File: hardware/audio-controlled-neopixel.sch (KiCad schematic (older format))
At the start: 63 parts, among them J1 AudioJack4, J2 AudioJack4, J3 KF2EDGK, J4 KF2EDGK, J5 KF2EDGK, J6 Conn_01x01_Female, J7 Conn_01x01_Female, J8 Conn_01x01_Female, J9 Conn_01x01_Female, SW1 SW_SPST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

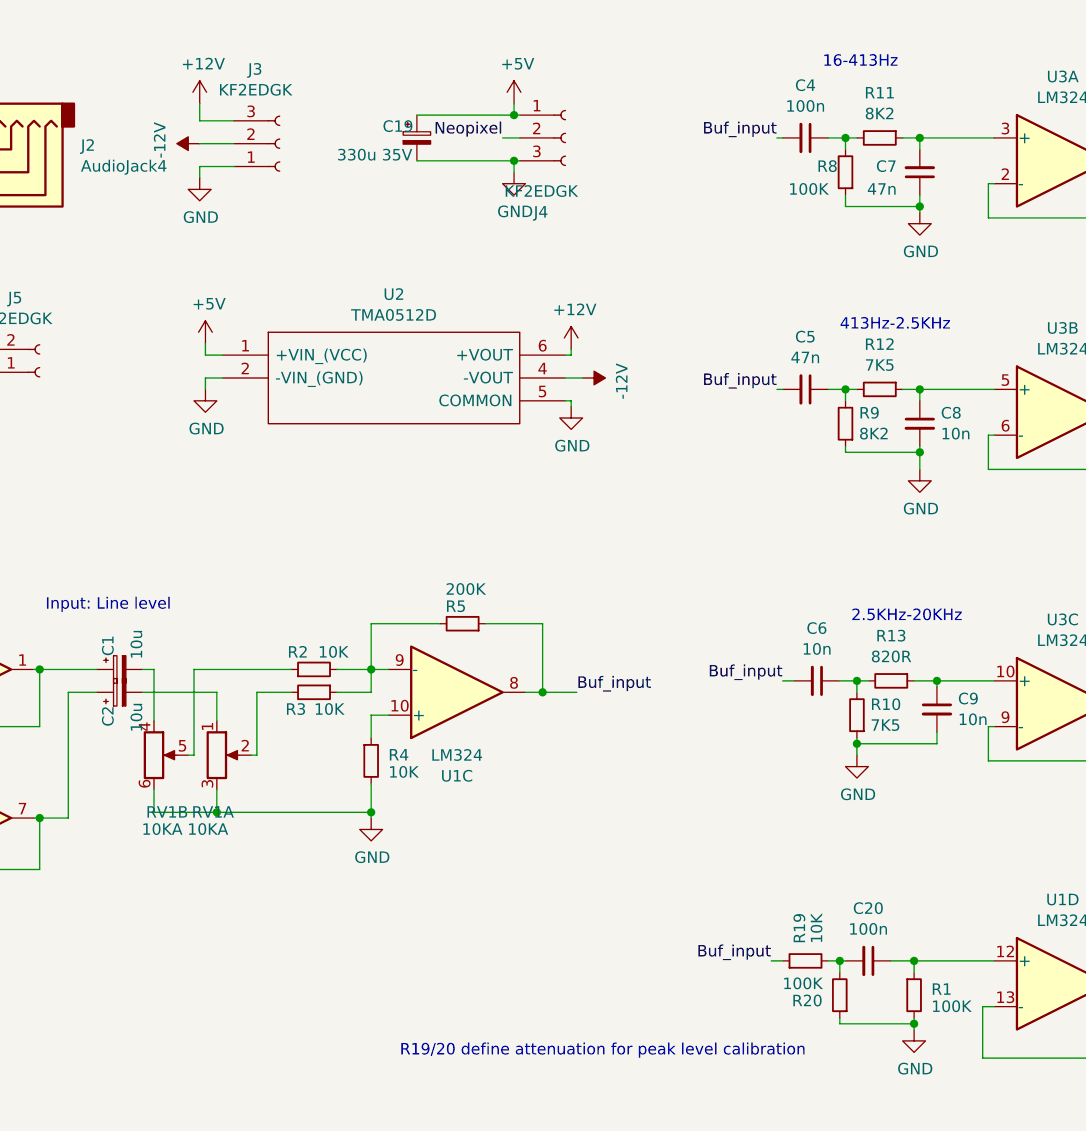
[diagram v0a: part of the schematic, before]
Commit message: added attenuators to keep frequency response flat
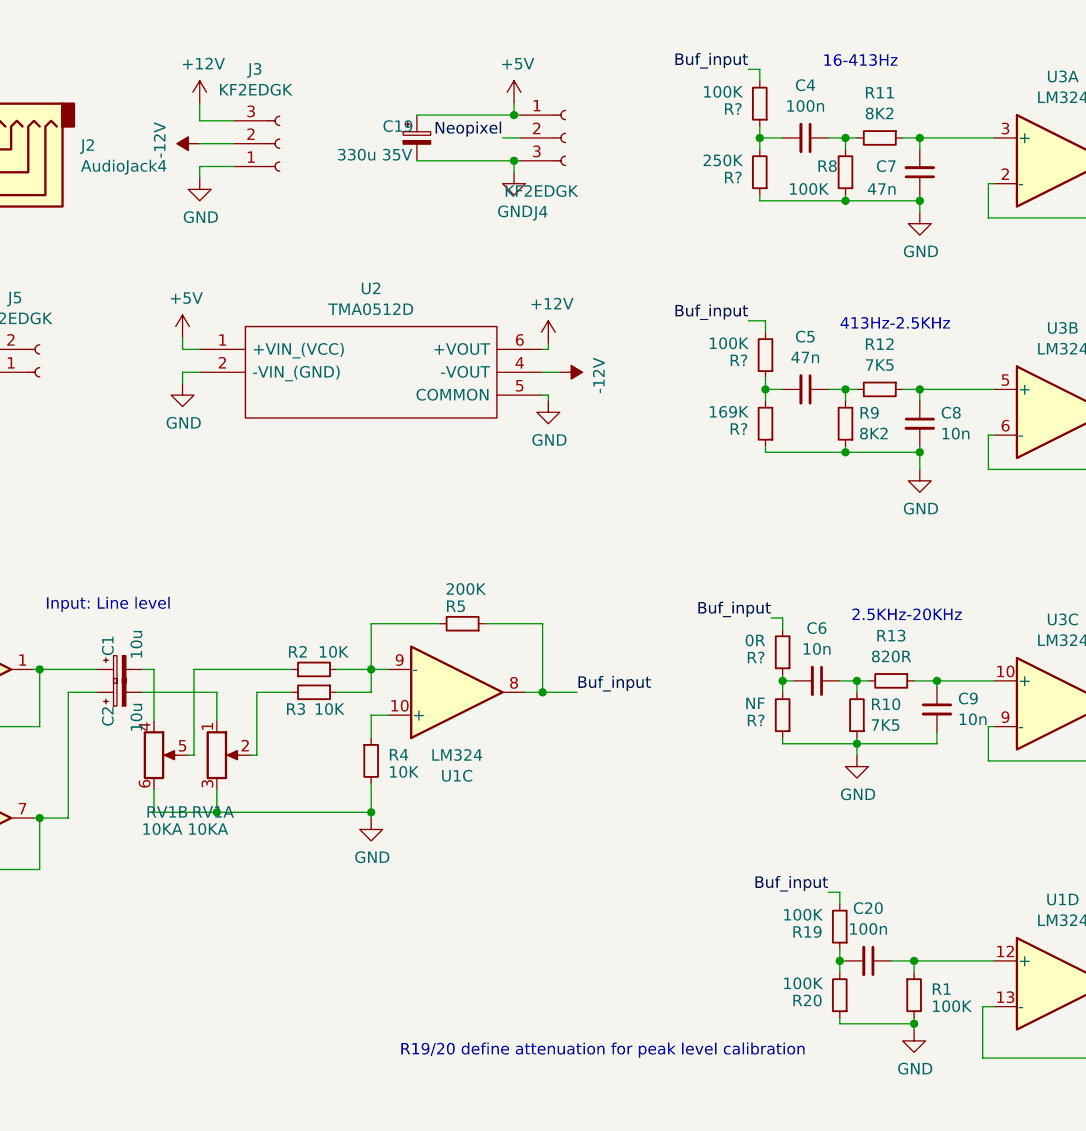
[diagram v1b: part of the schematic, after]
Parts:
- added R?: 0R, Resistor_SMD:R_0805_2012Metric, symbol Device:R_Small
- added R?: NF, Resistor_SMD:R_0805_2012Metric, symbol Device:R_Small
- added R? (x2): 100K, Resistor_SMD:R_0805_2012Metric, symbol Device:R_Small
- added R?: 169K, Resistor_SMD:R_0805_2012Metric, symbol Device:R_Small
- added R?: 250K, Resistor_SMD:R_0805_2012Metric, symbol Device:R_Small
- R19: value 10K -> 100K
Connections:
- net Buf_input: now also R19.2, R?.2, R?.2, R?.2; no longer C4.2, C5.2, C6.2, R19.1
- net GND: now also R?.1, R?.1, R?.1
- net at C20.2, R20.2: now also R19.1; no longer R19.2
- new net: C6.2, R?.1, R?.2
- new net: C5.2, R?.1, R?.2
- new net: C4.2, R?.1, R?.2
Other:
- moved on the sheet: R19, U2

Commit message: fixed library issue with schematic
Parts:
- U2: symbol TMA_2412D:TMA_2412D -> audio-controlled-neopixel-cache:TMA_2412D_TMA_2412D
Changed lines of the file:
@@
 EESchema Schematic File Version 4
+LIBS:audio-controlled-neopixel-cache
 EELAYER 26 0
 EELAYER END
@@
 Connection ~ 1200 1200
 $Comp
-L TMA_2412D:TMA_2412D U2
+L audio-controlled-neopixel-cache:TMA_2412D_TMA_2412D U2
 U 1 1 5C4B4FE3
 P 2450 1875

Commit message: added attenuators to balance frequency response
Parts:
- U2: footprint custom:TMA-0512D -> Footprints:TMAxxxxD; symbol audio-controlled-neopixel-cache:TMA_2412D_TMA_2412D -> audio-controlled-neopixel:custom_TMAxxxxD
- gave numbers to parts that had none: 6
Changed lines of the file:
@@
 L power:+12V #PWR0106
 U 1 1 5BF24254
-P 3975 1850
-F 0 "#PWR0106" H 3975 1700 50  0001 C CNN
-F 1 "+12V" H 3990 2023 50  0000 C CNN
-F 2 "" H 3975 1850 50  0001 C CNN
-F 3 "" H 3975 1850 50  0001 C CNN
-	1    3975 1850
+P 3475 1800
+F 0 "#PWR0106" H 3475 1650 50  0001 C CNN
+F 1 "+12V" H 3490 1973 50  0000 C CNN
+F 2 "" H 3475 1800 50  0001 C CNN
+F 3 "" H 3475 1800 50  0001 C CNN
+	1    3475 1800
 	1    0    0    -1
 $EndComp
@@
 L power:-12V #PWR0107
 U 1 1 5BF242D9
-P 4025 1975
-F 0 "#PWR0107" H 4025 2075 50  0001 C CNN
-F 1 "-12V" H 4040 2148 50  0000 C CNN
-F 2 "" H 4025 1975 50  0001 C CNN
-F 3 "" H 4025 1975 50  0001 C CNN
-	1    4025 1975
+P 3525 1925
+F 0 "#PWR0107" H 3525 2025 50  0001 C CNN
+F 1 "-12V" H 3540 2098 50  0000 C CNN
+F 2 "" H 3525 1925 50  0001 C CNN
+F 3 "" H 3525 1925 50  0001 C CNN
+	1    3525 1925
 	0    1    1    0
 $EndComp
 Wire Wire Line
-	3975 2100 3975 2075
-Wire Wire Line
-	3975 2075 3950 2075
-Wire Wire Line
-	3975 1850 3975 1875
-Wire Wire Line
-	3975 1875 3950 1875
-Wire Wire Line
-	3950 1975 4025 1975
+	3475 2050 3475 2025
+Wire Wire Line
+	3475 2025 3450 2025
+Wire Wire Line
+	3475 1800 3475 1825
+Wire Wire Line
+	3475 1825 3450 1825
+Wire Wire Line
+	3450 1925 3525 1925
 $Comp
 L Diode:BAT85 D3
@@
 L power:GND #PWR0111
 U 1 1 5C0E2BC2
-P 3975 2100
-F 0 "#PWR0111" H 3975 1850 50  0001 C CNN
-F 1 "GND" H 3980 1927 50  0000 C CNN
-F 2 "" H 3975 2100 50  0001 C CNN
-F 3 "" H 3975 2100 50  0001 C CNN
-	1    3975 2100
+P 3475 2050
+F 0 "#PWR0111" H 3475 1800 50  0001 C CNN
+F 1 "GND" H 3480 1877 50  0000 C CNN
+F 2 "" H 3475 2050 50  0001 C CNN
+F 3 "" H 3475 2050 50  0001 C CNN
+	1    3475 2050
 	1    0    0    -1
 $EndComp
@@
 	1400 1200 1200 1200
 Connection ~ 1200 1200
-$Comp
-L audio-controlled-neopixel-cache:TMA_2412D_TMA_2412D U2
-U 1 1 5C4B4FE3
-P 2450 1875
-F 0 "U2" H 3200 2140 50  0000 C CNN
-F 1 "TMA0512D" H 3200 2049 50  0000 C CNN
-F 2 "custom:TMA-0512D" H 3800 1975 50  0001 L CNN
-F 3 "http://docs-emea.rs-online.com/webdocs/0e18/0900766b80e182f0.pdf" H 3800 1875 50  0001 L CNN
-F 4 "TMA2412D unregulated DC-DC,+/-12V 1W 1W Isolated DC-DC Converter, Vin 21.6" H 3800 1775 50  0001 L CNN "Description"
-F 5 "Traco Power" H 3800 1575 50  0001 L CNN "Manufacturer_Name"
-F 6 "TMA 2412D" H 3800 1475 50  0001 L CNN "Manufacturer_Part_Number"
-F 7 "1247598" H 3800 1375 50  0001 L CNN "RS Part Number"
-F 8 "http://uk.rs-online.com/web/p/products/1247598" H 3800 1275 50  0001 L CNN "RS Price/Stock"
-F 9 "495-TMA-2412D" H 3800 1175 50  0001 L CNN "Mouser Part Number"
-F 10 "https://www.mouser.com/Search/Refine.aspx?Keyword=495-TMA-2412D" H 3800 1075 50  0001 L CNN "Mouser Price/Stock"
-	1    2450 1875
-	1    0    0    -1
-$EndComp
 Text Label 4950 3050 2    50   ~ 0
 Buf_input
 $Comp
-L Device:R_Small R?
+L Device:R_Small R25
 U 1 1 5C4F25BC
 P 5000 3200
-F 0 "R?" H 5075 3225 50  0000 L CNN
+F 0 "R25" H 5075 3225 50  0000 L CNN
 F 1 "0R" H 5075 3150 50  0000 L CNN
 F 2 "Resistor_SMD:R_0805_2012Metric" H 5000 3200 50  0001 C CNN
@@
 $EndComp
 $Comp
-L Device:R_Small R?
+L Device:R_Small R26
 U 1 1 5C4F25C3
 P 5000 3475
-F 0 "R?" H 5075 3500 50  0000 L CNN
+F 0 "R26" H 5075 3500 50  0000 L CNN
 F 1 "NF" H 5075 3425 50  0000 L CNN
 F 2 "Resistor_SMD:R_0805_2012Metric" H 5000 3475 50  0001 C CNN
@@
 Buf_input
 $Comp
-L Device:R_Small R?
+L Device:R_Small R23
 U 1 1 5C53A2E4
 P 4925 1900
-F 0 "R?" H 5000 1925 50  0000 L CNN
+F 0 "R23" H 5000 1925 50  0000 L CNN
 F 1 "100K" H 5000 1850 50  0000 L CNN
 F 2 "Resistor_SMD:R_0805_2012Metric" H 4925 1900 50  0001 C CNN
@@
 $EndComp
 $Comp
-L Device:R_Small R?
+L Device:R_Small R24
 U 1 1 5C53A2EA
 P 4925 2200
-F 0 "R?" H 5000 2225 50  0000 L CNN
+F 0 "R24" H 5000 2225 50  0000 L CNN
 F 1 "169K" H 5000 2150 50  0000 L CNN
 F 2 "Resistor_SMD:R_0805_2012Metric" H 4925 2200 50  0001 C CNN
@@
 Buf_input
 $Comp
-L Device:R_Small R?
+L Device:R_Small R21
 U 1 1 5C5862DE
 P 4900 800
-F 0 "R?" H 4975 825 50  0000 L CNN
+F 0 "R21" H 4975 825 50  0000 L CNN
 F 1 "100K" H 4975 750 50  0000 L CNN
 F 2 "Resistor_SMD:R_0805_2012Metric" H 4900 800 50  0001 C CNN
@@
 $EndComp
 $Comp
-L Device:R_Small R?
+L Device:R_Small R22
 U 1 1 5C5862E4
 P 4900 1100
-F 0 "R?" H 4975 1125 50  0000 L CNN
+F 0 "R22" H 4975 1125 50  0000 L CNN
 F 1 "250K" H 4975 1050 50  0000 L CNN
 F 2 "Resistor_SMD:R_0805_2012Metric" H 4900 1100 50  0001 C CNN
@@
 Wire Wire Line
 	5250 4250 5250 4300
+$Comp
+L audio-controlled-neopixel:custom_TMAxxxxD U2
+U 1 1 5C4B4FE3
+P 2950 2075
+F 0 "U2" H 2775 1725 50  0000 C CNN
+F 1 "TMA0512D" H 3025 1950 50  0000 C CNN
+F 2 "Footprints:TMAxxxxD" H 4300 2175 50  0001 L CNN
+F 3 "http://docs-emea.rs-online.com/webdocs/0e18/0900766b80e182f0.pdf" H 4300 2075 50  0001 L CNN
+F 4 "TMA2412D unregulated DC-DC,+/-12V 1W 1W Isolated DC-DC Converter, Vin 21.6" H 4300 1975 50  0001 L CNN "Description"
+F 5 "Traco Power" H 4300 1775 50  0001 L CNN "Manufacturer_Name"
+F 6 "TMA 2412D" H 4300 1675 50  0001 L CNN "Manufacturer_Part_Number"
+F 7 "1247598" H 4300 1575 50  0001 L CNN "RS Part Number"
+F 8 "http://uk.rs-online.com/web/p/products/1247598" H 4300 1475 50  0001 L CNN "RS Price/Stock"
+F 9 "495-TMA-2412D" H 4300 1375 50  0001 L CNN "Mouser Part Number"
+F 10 "https://www.mouser.com/Search/Refine.aspx?Keyword=495-TMA-2412D" H 4300 1275 50  0001 L CNN "Mouser Price/Stock"
+	1    2950 2075
+	1    0    0    -1
+$EndComp
 $EndSCHEMATC

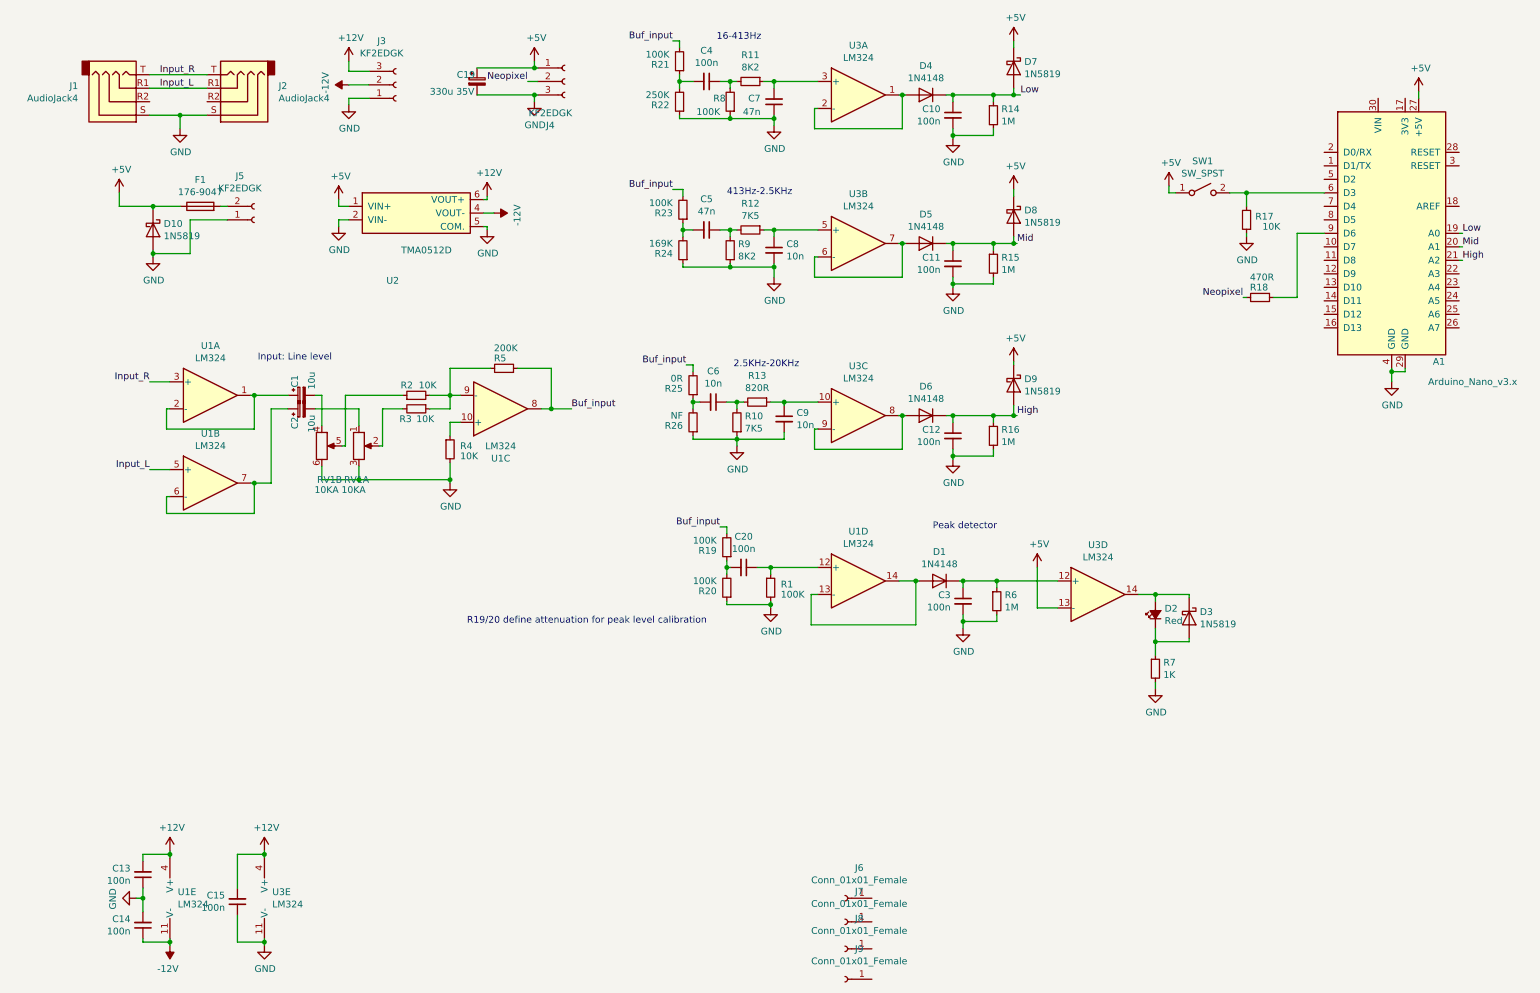
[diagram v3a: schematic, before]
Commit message: removed analogue clipping hardware to prepare for transisiton to software solution (not implemented)
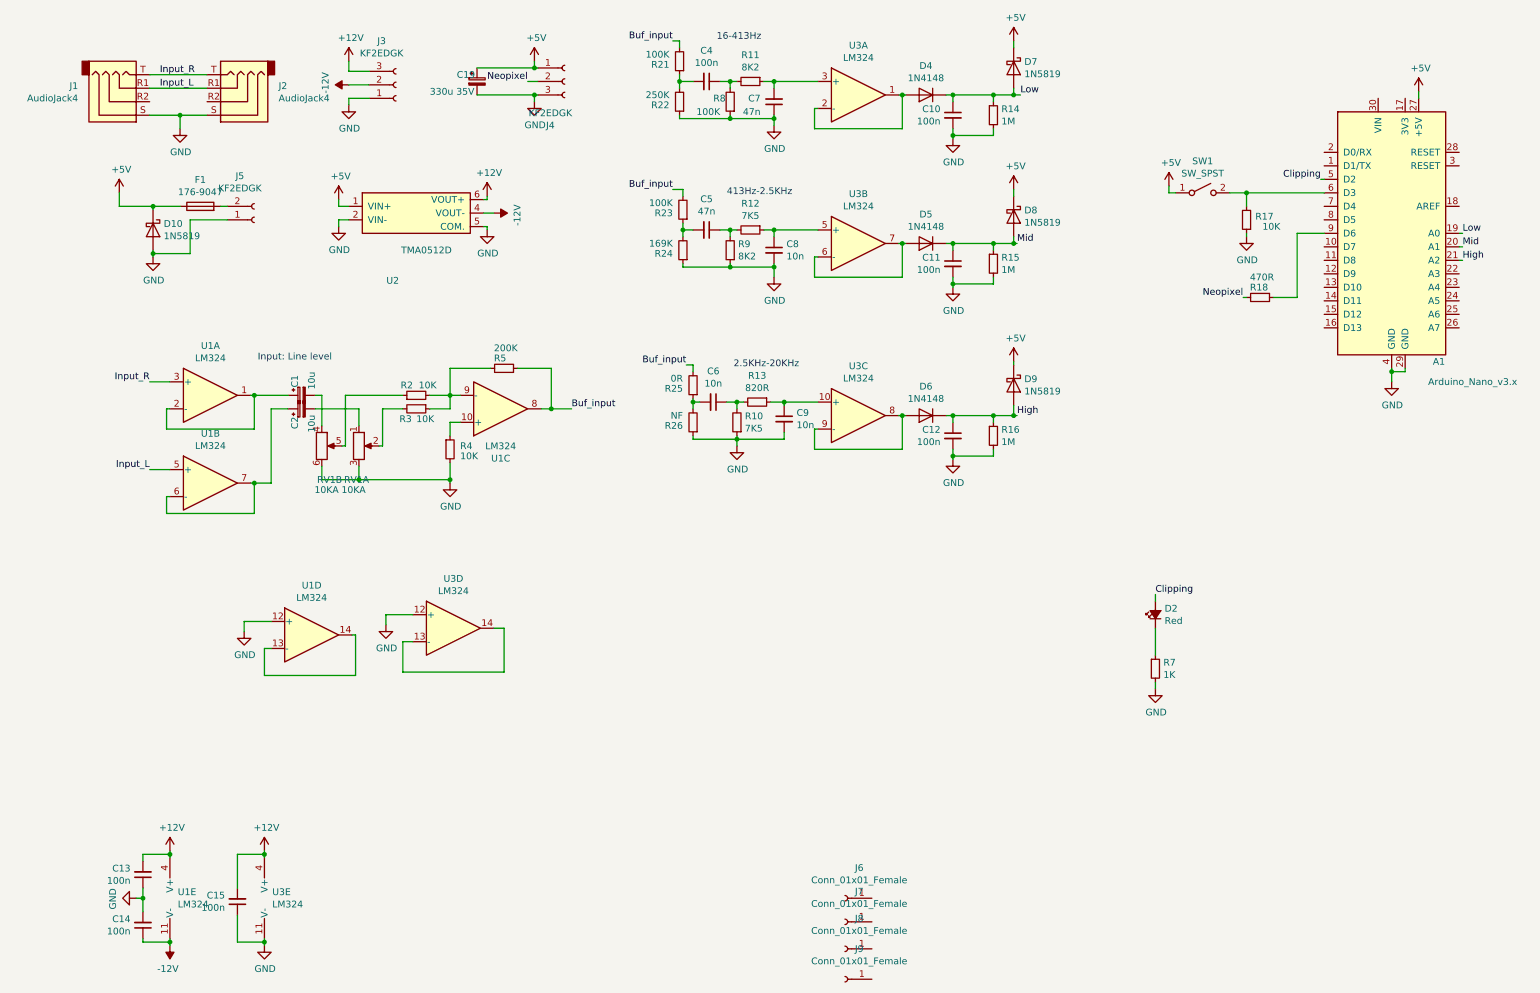
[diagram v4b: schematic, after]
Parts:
- removed C20, C3: 100n, Capacitor_SMD:C_0805_2012Metric, symbol Device:C_Small
- removed D1: 1N4148, Diode_SMD:D_SOD-123, symbol Diode:1N4148
- removed D3: 1N5819, Diode_SMD:D_SOD-123, symbol Diode:BAT85
- removed R1, R19, R20: 100K, Resistor_SMD:R_0805_2012Metric, symbol Device:R_Small
- removed R6: 1M, Resistor_SMD:R_0805_2012Metric, symbol Device:R_Small
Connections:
- net +5V: no longer U3.13 (-)
- net GND: now also U1.12 (+), U3.12 (+)
- net Clipping: now reaches A1.5 (D2)
- net Clipping: now also D2.2 (A)
- net at U3.14: now also U3.13 (-); no longer D2.2 (A)
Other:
- note removed: "Peak detector"
- note removed: "R19/20 define attenuation for peak level calibration"

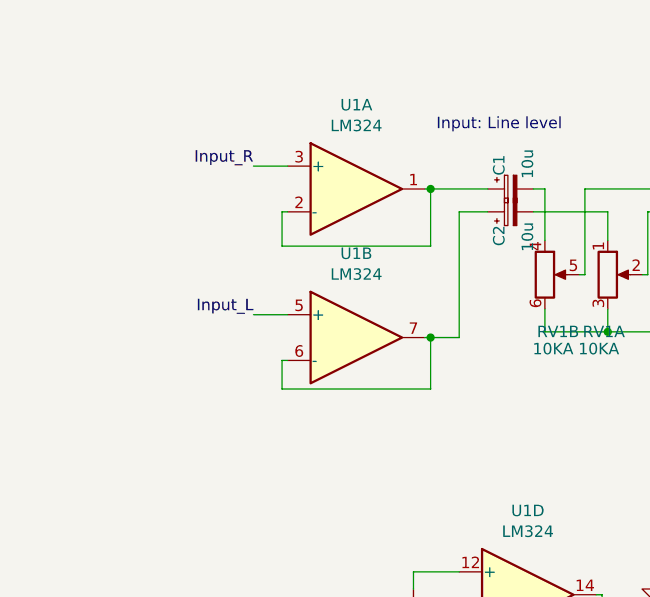
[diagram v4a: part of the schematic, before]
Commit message: added input resistors
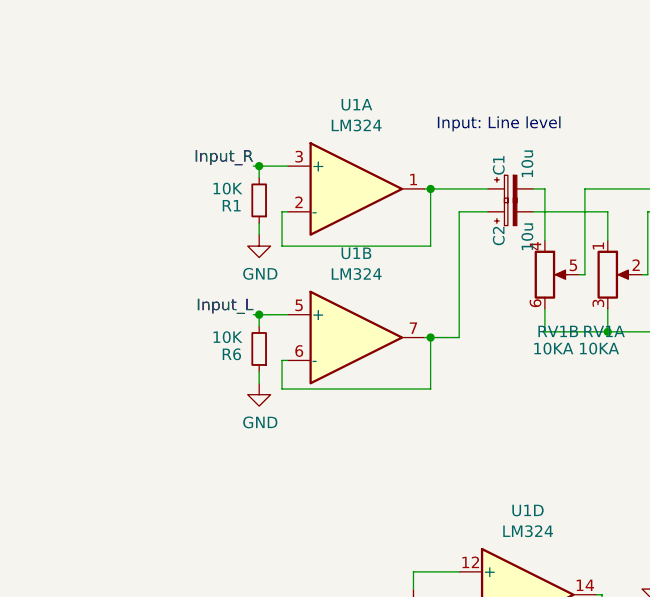
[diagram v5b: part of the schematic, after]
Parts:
- added R1, R6: 10K, Resistor_SMD:R_0805_2012Metric, symbol Device:R_Small
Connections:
- net GND: now also R1.1, R6.1
- net Input_L: now also R6.2
- net Input_R: now also R1.2
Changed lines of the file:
@@
 Input_R
 Wire Wire Line
-	975  3175 1125 3175
-Wire Wire Line
-	975  3825 1125 3825
+	975  3175 1000 3175
+Wire Wire Line
+	975  3825 1000 3825
 Wire Wire Line
 	1725 3275 1750 3275
@@
 Wire Wire Line
 	1675 4950 1675 5025
+$Comp
+L Device:R_Small R6
+U 1 1 5C673748
+P 1000 3975
+F 0 "R6" H 1075 4000 50  0000 L CNN
+F 1 "10K" H 1075 3925 50  0000 L CNN
+F 2 "Resistor_SMD:R_0805_2012Metric" H 1000 3975 50  0001 C CNN
+F 3 "~" H 1000 3975 50  0001 C CNN
+	1    1000 3975
+	-1   0    0    1
+$EndComp
+$Comp
+L Device:R_Small R1
+U 1 1 5C673892
+P 1000 3325
+F 0 "R1" H 1075 3350 50  0000 L CNN
+F 1 "10K" H 1075 3275 50  0000 L CNN
+F 2 "Resistor_SMD:R_0805_2012Metric" H 1000 3325 50  0001 C CNN
+F 3 "~" H 1000 3325 50  0001 C CNN
+	1    1000 3325
+	-1   0    0    1
+$EndComp
+$Comp
+L power:GND #PWR0128
+U 1 1 5C673948
+P 1000 3475
+F 0 "#PWR0128" H 1000 3225 50  0001 C CNN
+F 1 "GND" H 1005 3302 50  0000 C CNN
+F 2 "" H 1000 3475 50  0001 C CNN
+F 3 "" H 1000 3475 50  0001 C CNN
+	1    1000 3475
+	1    0    0    -1
+$EndComp
+$Comp
+L power:GND #PWR0129
+U 1 1 5C6739E3
+P 1000 4125
+F 0 "#PWR0129" H 1000 3875 50  0001 C CNN
+F 1 "GND" H 1005 3952 50  0000 C CNN
+F 2 "" H 1000 4125 50  0001 C CNN
+F 3 "" H 1000 4125 50  0001 C CNN
+	1    1000 4125
+	1    0    0    -1
+$EndComp
+Wire Wire Line
+	1000 3225 1000 3175
+Connection ~ 1000 3175
+Wire Wire Line
+	1000 3175 1125 3175
+Wire Wire Line
+	1000 3475 1000 3425
+Wire Wire Line
+	1000 3875 1000 3825
+Connection ~ 1000 3825
+Wire Wire Line
+	1000 3825 1125 3825
+Wire Wire Line
+	1000 4075 1000 4125
 $EndSCHEMATC
